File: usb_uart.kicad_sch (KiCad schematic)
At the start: 18 parts, among them J9 USB_C_Receptacle_2.0, U20 CP2102N-A01-GQFN28, U25 CM1293A-04SO

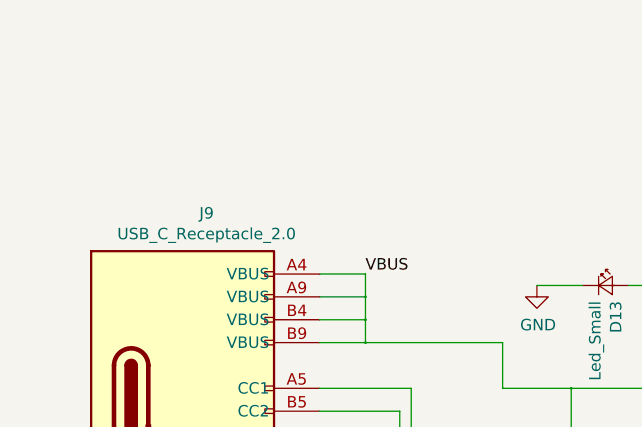
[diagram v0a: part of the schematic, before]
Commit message: Fixed bypass capacitor positions; DRC clear
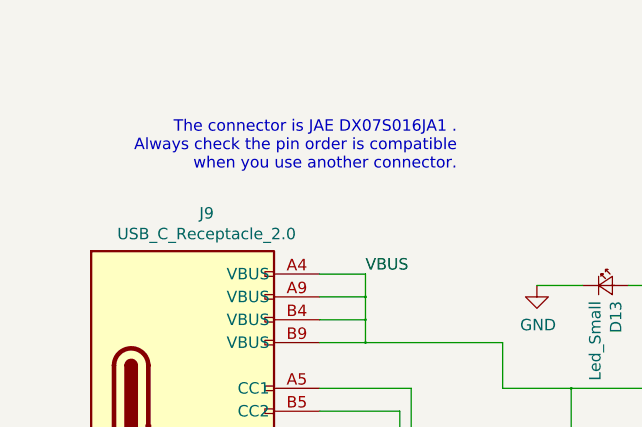
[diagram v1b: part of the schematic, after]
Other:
- note added: "The connector is JAE DX07S016JA1 . Always check the pin order is compatible when you use another connector."
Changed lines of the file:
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@@
-(kicad_sch (version 20200820) (host eeschema "5.99.0-unknown-dd374e12a~102~ubuntu18.04.1")
+(kicad_sch (version 20200820) (host eeschema "5.99.0-unknown-b0af66afc~103~ubuntu18.04.1")
   (page 10 10)
   (paper "A4")
@@
   (junction (at 113.03 54.61) (diameter 0.3048) (color 0 0 0 0))
   (junction (at 135.89 31.75) (diameter 0.3048) (color 0 0 0 0))
-  (no_connect (at 153.67 57.15))
-  (no_connect (at 154.94 64.77))
+  (no_connect (at 153.67 39.37))
+  (no_connect (at 154.94 62.23))
+  (no_connect (at 123.19 46.99))
+  (no_connect (at 153.67 77.47))
+  (no_connect (at 153.67 41.91))
+  (no_connect (at 154.94 67.31))
+  (no_connect (at 153.67 74.93))
+  (no_connect (at 40.64 77.47))
   (no_connect (at 40.64 80.01))
-  (no_connect (at 153.67 77.47))
   (no_connect (at 154.94 59.69))
   (no_connect (at 153.67 52.07))
-  (no_connect (at 123.19 46.99))
-  (no_connect (at 154.94 67.31))
+  (no_connect (at 154.94 69.85))
+  (no_connect (at 154.94 64.77))
+  (no_connect (at 153.67 72.39))
   (no_connect (at 153.67 80.01))
-  (no_connect (at 40.64 77.47))
-  (no_connect (at 153.67 39.37))
-  (no_connect (at 154.94 62.23))
-  (no_connect (at 153.67 72.39))
-  (no_connect (at 153.67 74.93))
-  (no_connect (at 154.94 69.85))
-  (no_connect (at 153.67 41.91))
+  (no_connect (at 153.67 57.15))
   (wire (pts (xy 17.78 87.63) (xy 17.78 91.44))
     (stroke (width 0) (type solid) (color 0 0 0 0))
@@
     (effects (font (size 1.27 1.27)) (justify right bottom))
   )
+  (text "The connector is JAE DX07S016JA1 .\nAlways check the pin order is compatible\nwhen you use another connector."
+    (at 55.88 34.29 0)
+    (effects (font (size 1.27 1.27)) (justify right bottom))
+  )

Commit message: Added some comments
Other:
- note added: "3mm at light speed requires a time to travel of : 0.01 ns A time needed by one phase of 12MHz wave : 83.33 ns Therefore, 3mm length mismatch is negligible at this transmission speed. Don't stick to the length matching so much."
- note removed: "3mm at light speed requires a time to travel of : 0.01 ns A time needed by one phase of 12MHz wave : 83.33 ns Therefore, 3mm length mismatch is negligible at this transmission speed."
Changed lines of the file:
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@@
-(kicad_sch (version 20200820) (host eeschema "5.99.0-unknown-b0af66afc~103~ubuntu18.04.1")
+(kicad_sch (version 20200827) (generator eeschema)
   (page 10 10)
   (paper "A4")
@@
   (junction (at 113.03 54.61) (diameter 0.3048) (color 0 0 0 0))
   (junction (at 135.89 31.75) (diameter 0.3048) (color 0 0 0 0))
-  (no_connect (at 154.94 59.69))
+  (no_connect (at 153.67 72.39))
+  (no_connect (at 154.94 67.31))
+  (no_connect (at 153.67 41.91))
+  (no_connect (at 153.67 52.07))
   (no_connect (at 154.94 64.77))
   (no_connect (at 153.67 57.15))
-  (no_connect (at 154.94 69.85))
-  (no_connect (at 153.67 52.07))
+  (no_connect (at 153.67 77.47))
+  (no_connect (at 40.64 80.01))
+  (no_connect (at 154.94 59.69))
+  (no_connect (at 153.67 80.01))
+  (no_connect (at 153.67 39.37))
+  (no_connect (at 40.64 77.47))
   (no_connect (at 123.19 46.99))
   (no_connect (at 153.67 74.93))
-  (no_connect (at 153.67 72.39))
-  (no_connect (at 154.94 67.31))
   (no_connect (at 154.94 62.23))
-  (no_connect (at 40.64 77.47))
-  (no_connect (at 40.64 80.01))
-  (no_connect (at 153.67 39.37))
-  (no_connect (at 153.67 41.91))
-  (no_connect (at 153.67 80.01))
-  (no_connect (at 153.67 77.47))
+  (no_connect (at 154.94 69.85))
   (wire (pts (xy 17.78 87.63) (xy 17.78 91.44))
     (stroke (width 0) (type solid) (color 0 0 0 0))
@@
     (effects (font (size 1.27 1.27)) (justify right bottom))
   )
-  (text "3mm at light speed requires a time to travel of : 0.01 ns\nA time needed by one phase of 12MHz wave  : 83.33 ns\n\nTherefore, 3mm length mismatch is negligible at this transmission speed.  "
-    (at 143.51 123.19 0)
-    (effects (font (size 1.27 1.27)) (justify right bottom))
+  (text "3mm at light speed requires a time to travel of : 0.01 ns\nA time needed by one phase of 12MHz wave  : 83.33 ns\n\nTherefore, 3mm length mismatch is negligible at this transmission speed.  \nDon't stick to the length matching so much."
+    (at 82.55 123.19 0)
+    (effects (font (size 1.27 1.27)) (justify left bottom))
   )
   (label "VBUS" (at 45.72 45.72 0)

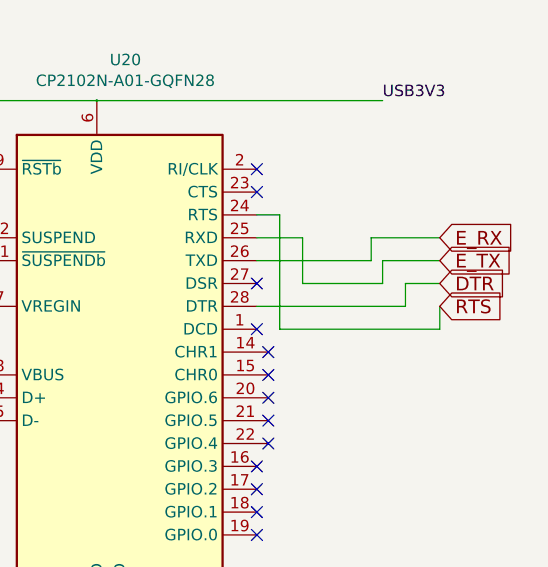
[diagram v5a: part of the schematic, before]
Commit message: Fixed some comments; Added FB on SCL/SDA line
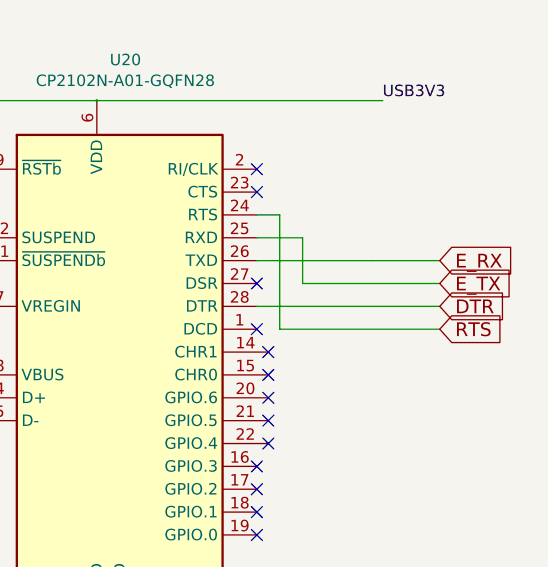
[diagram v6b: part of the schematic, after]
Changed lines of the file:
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@@
   (junction (at 113.03 54.61) (diameter 0.3048) (color 0 0 0 0))
   (junction (at 135.89 31.75) (diameter 0.3048) (color 0 0 0 0))
+  (no_connect (at 153.67 77.47))
+  (no_connect (at 40.64 77.47))
+  (no_connect (at 154.94 67.31))
+  (no_connect (at 153.67 74.93))
+  (no_connect (at 154.94 59.69))
+  (no_connect (at 153.67 52.07))
+  (no_connect (at 123.19 46.99))
+  (no_connect (at 153.67 80.01))
+  (no_connect (at 154.94 62.23))
+  (no_connect (at 153.67 39.37))
   (no_connect (at 153.67 72.39))
-  (no_connect (at 154.94 67.31))
   (no_connect (at 153.67 41.91))
-  (no_connect (at 153.67 52.07))
+  (no_connect (at 40.64 80.01))
   (no_connect (at 154.94 64.77))
+  (no_connect (at 154.94 69.85))
   (no_connect (at 153.67 57.15))
-  (no_connect (at 153.67 77.47))
-  (no_connect (at 40.64 80.01))
-  (no_connect (at 154.94 59.69))
-  (no_connect (at 153.67 80.01))
-  (no_connect (at 153.67 39.37))
-  (no_connect (at 40.64 77.47))
-  (no_connect (at 123.19 46.99))
-  (no_connect (at 153.67 74.93))
-  (no_connect (at 154.94 62.23))
-  (no_connect (at 154.94 69.85))
   (wire (pts (xy 17.78 87.63) (xy 17.78 91.44))
     (stroke (width 0) (type solid) (color 0 0 0 0))
@@
     (stroke (width 0) (type solid) (color 0 0 0 0))
   )
+  (wire (pts (xy 156.21 57.15) (xy 173.99 57.15))
+    (stroke (width 0) (type solid) (color 0 0 0 0))
+  )
   (wire (pts (xy 158.75 46.99) (xy 153.67 46.99))
     (stroke (width 0) (type solid) (color 0 0 0 0))
@@
     (stroke (width 0) (type solid) (color 0 0 0 0))
   )
-  (wire (pts (xy 166.37 46.99) (xy 166.37 49.53))
-    (stroke (width 0) (type solid) (color 0 0 0 0))
-  )
   (wire (pts (xy 166.37 49.53) (xy 153.67 49.53))
     (stroke (width 0) (type solid) (color 0 0 0 0))
   )
+  (wire (pts (xy 166.37 49.53) (xy 173.99 49.53))
+    (stroke (width 0) (type solid) (color 0 0 0 0))
+  )
   (wire (pts (xy 167.64 31.75) (xy 135.89 31.75))
     (stroke (width 0) (type solid) (color 0 0 0 0))
   )
-  (wire (pts (xy 167.64 49.53) (xy 167.64 52.07))
-    (stroke (width 0) (type solid) (color 0 0 0 0))
-  )
   (wire (pts (xy 167.64 52.07) (xy 158.75 52.07))
     (stroke (width 0) (type solid) (color 0 0 0 0))
   )
-  (wire (pts (xy 170.18 52.07) (xy 170.18 54.61))
+  (wire (pts (xy 167.64 52.07) (xy 173.99 52.07))
     (stroke (width 0) (type solid) (color 0 0 0 0))
   )
@@
     (stroke (width 0) (type solid) (color 0 0 0 0))
   )
-  (wire (pts (xy 173.99 46.99) (xy 166.37 46.99))
-    (stroke (width 0) (type solid) (color 0 0 0 0))
-  )
-  (wire (pts (xy 173.99 49.53) (xy 167.64 49.53))
-    (stroke (width 0) (type solid) (color 0 0 0 0))
-  )
-  (wire (pts (xy 173.99 52.07) (xy 170.18 52.07))
-    (stroke (width 0) (type solid) (color 0 0 0 0))
-  )
-  (wire (pts (xy 173.99 54.61) (xy 173.99 57.15))
-    (stroke (width 0) (type solid) (color 0 0 0 0))
-  )
-  (wire (pts (xy 173.99 57.15) (xy 156.21 57.15))
+  (wire (pts (xy 170.18 54.61) (xy 173.99 54.61))
     (stroke (width 0) (type solid) (color 0 0 0 0))
   )
@@
     (effects (font (size 1.27 1.27)) (justify left bottom))
   )
-  (global_label "E_RX" (shape input) (at 173.99 46.99 0)
+  (global_label "E_RX" (shape input) (at 173.99 49.53 0)
     (effects (font (size 1.524 1.524)) (justify left))
   )
-  (global_label "E_TX" (shape input) (at 173.99 49.53 0)
+  (global_label "E_TX" (shape input) (at 173.99 52.07 0)
     (effects (font (size 1.524 1.524)) (justify left))
   )
-  (global_label "DTR" (shape input) (at 173.99 52.07 0)
+  (global_label "DTR" (shape input) (at 173.99 54.61 0)
     (effects (font (size 1.524 1.524)) (justify left))
   )
-  (global_label "RTS" (shape input) (at 173.99 54.61 0)
+  (global_label "RTS" (shape input) (at 173.99 57.15 0)
     (effects (font (size 1.524 1.524)) (justify left))
   )

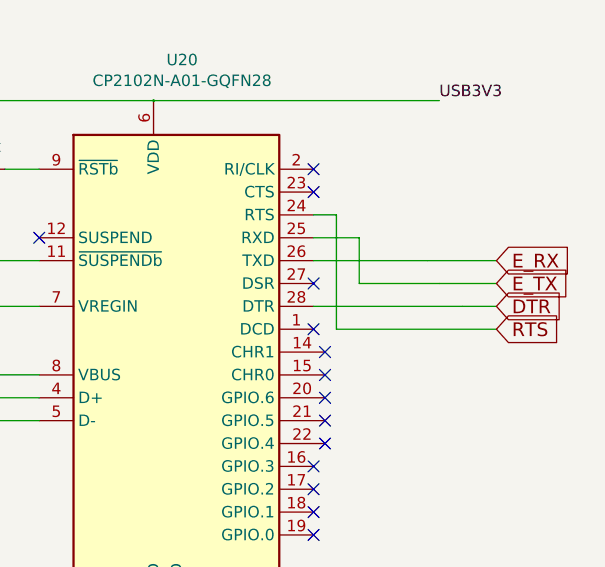
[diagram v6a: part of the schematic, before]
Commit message: Re-arranged physical buttions; DRC clear
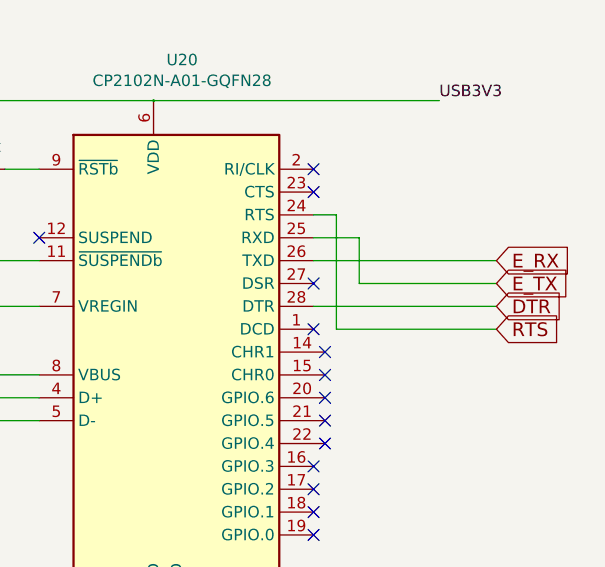
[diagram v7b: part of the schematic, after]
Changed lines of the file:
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@@
-(kicad_sch (version 20200827) (generator eeschema)
+(kicad_sch (version 20200828) (generator eeschema)
   (page 10 10)
   (paper "A4")
@@
   (junction (at 113.03 54.61) (diameter 0.3048) (color 0 0 0 0))
   (junction (at 135.89 31.75) (diameter 0.3048) (color 0 0 0 0))
+  (no_connect (at 40.64 80.01))
+  (no_connect (at 153.67 39.37))
   (no_connect (at 153.67 77.47))
+  (no_connect (at 154.94 67.31))
+  (no_connect (at 153.67 57.15))
+  (no_connect (at 153.67 52.07))
+  (no_connect (at 154.94 69.85))
+  (no_connect (at 153.67 72.39))
+  (no_connect (at 154.94 62.23))
+  (no_connect (at 154.94 64.77))
   (no_connect (at 40.64 77.47))
-  (no_connect (at 154.94 67.31))
+  (no_connect (at 153.67 41.91))
+  (no_connect (at 153.67 80.01))
   (no_connect (at 153.67 74.93))
   (no_connect (at 154.94 59.69))
-  (no_connect (at 153.67 52.07))
   (no_connect (at 123.19 46.99))
-  (no_connect (at 153.67 80.01))
-  (no_connect (at 154.94 62.23))
-  (no_connect (at 153.67 39.37))
-  (no_connect (at 153.67 72.39))
-  (no_connect (at 153.67 41.91))
-  (no_connect (at 40.64 80.01))
-  (no_connect (at 154.94 64.77))
-  (no_connect (at 154.94 69.85))
-  (no_connect (at 153.67 57.15))
   (wire (pts (xy 17.78 87.63) (xy 17.78 91.44))
     (stroke (width 0) (type solid) (color 0 0 0 0))
@@
     (stroke (width 0) (type solid) (color 0 0 0 0))
   )
+  (wire (pts (xy 153.67 49.53) (xy 173.99 49.53))
+    (stroke (width 0) (type solid) (color 0 0 0 0))
+  )
+  (wire (pts (xy 153.67 54.61) (xy 173.99 54.61))
+    (stroke (width 0) (type solid) (color 0 0 0 0))
+  )
   (wire (pts (xy 156.21 44.45) (xy 153.67 44.45))
     (stroke (width 0) (type solid) (color 0 0 0 0))
@@
     (stroke (width 0) (type solid) (color 0 0 0 0))
   )
-  (wire (pts (xy 166.37 49.53) (xy 153.67 49.53))
-    (stroke (width 0) (type solid) (color 0 0 0 0))
-  )
-  (wire (pts (xy 166.37 49.53) (xy 173.99 49.53))
+  (wire (pts (xy 158.75 52.07) (xy 173.99 52.07))
     (stroke (width 0) (type solid) (color 0 0 0 0))
   )
@@
     (stroke (width 0) (type solid) (color 0 0 0 0))
   )
-  (wire (pts (xy 167.64 52.07) (xy 158.75 52.07))
-    (stroke (width 0) (type solid) (color 0 0 0 0))
-  )
-  (wire (pts (xy 167.64 52.07) (xy 173.99 52.07))
-    (stroke (width 0) (type solid) (color 0 0 0 0))
-  )
-  (wire (pts (xy 170.18 54.61) (xy 153.67 54.61))
-    (stroke (width 0) (type solid) (color 0 0 0 0))
-  )
-  (wire (pts (xy 170.18 54.61) (xy 173.99 54.61))
-    (stroke (width 0) (type solid) (color 0 0 0 0))
-  )
